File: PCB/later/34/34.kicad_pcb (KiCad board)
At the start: 2 copper layers, 112.4 x 93.3 mm, 61 parts, among them J1 USB_C_Receptacle_USB2.0, J2 Conn_01x04, J3 AVR-ISP-6, J4 Conn_01x04, SW1 SW_Push, SW10 SW_Push, SW11 SW_Push, SW12 SW_Push, SW13 SW_Push, SW14 SW_Push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

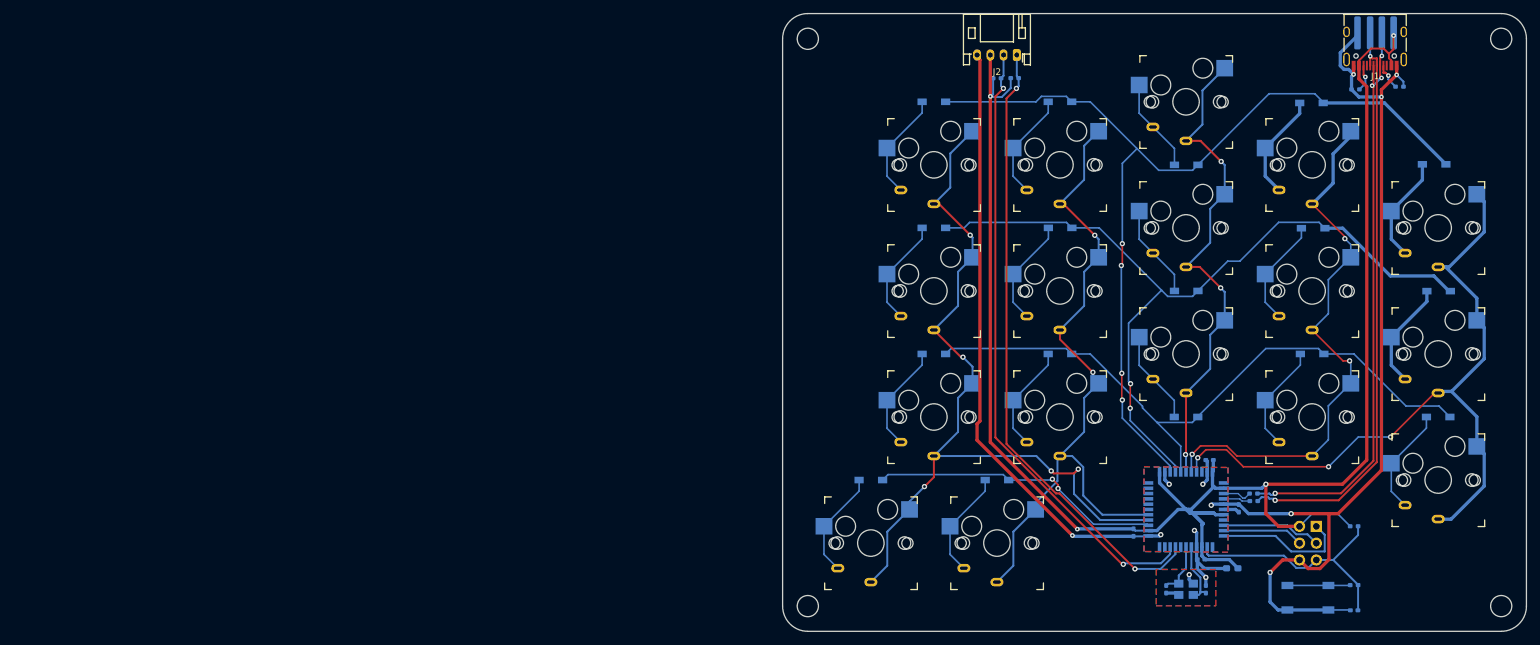
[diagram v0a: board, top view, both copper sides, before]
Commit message: postpone i2c design
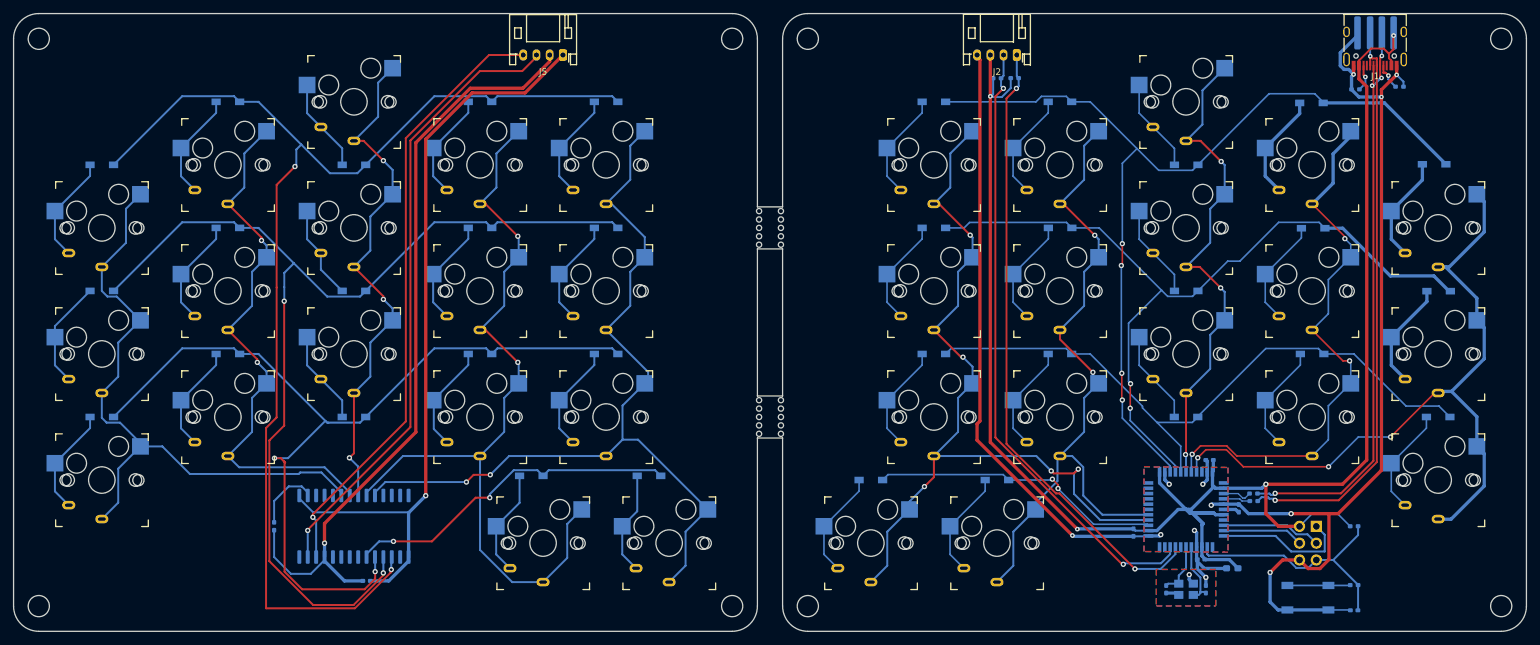
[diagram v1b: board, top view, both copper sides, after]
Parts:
- added C9: 0.1µF, Capacitor_SMD:C_0402_1005Metric_Pad0.74x0.62mm_HandSolder, B.Cu at (91.4, 131.4)
- added D18: 1N4148, Keyboard_Foostan:D3_SMD_v2, B.Cu at (51.4, 68.6)
- added D19: 1N4148, Keyboard_Foostan:D3_SMD_v2, B.Cu at (51.4, 87.6)
- added D20: 1N4148, Keyboard_Foostan:D3_SMD_v2, B.Cu at (51.4, 106.7)
- added D21: 1N4148, Keyboard_Foostan:D3_SMD_v2, B.Cu at (70.5, 59.1)
- added D22: 1N4148, Keyboard_Foostan:D3_SMD_v2, B.Cu at (70.5, 78.1)
- added D23: 1N4148, Keyboard_Foostan:D3_SMD_v2, B.Cu at (70.5, 97.2)
- added D24: 1N4148, Keyboard_Foostan:D3_SMD_v2, B.Cu at (89.5, 68.6)
- added D25: 1N4148, Keyboard_Foostan:D3_SMD_v2, B.Cu at (89.5, 87.6)
- added D26: 1N4148, Keyboard_Foostan:D3_SMD_v2, B.Cu at (89.5, 106.7)
- added D27: 1N4148, Keyboard_Foostan:D3_SMD_v2, B.Cu at (108.6, 59.1)
- added D28: 1N4148, Keyboard_Foostan:D3_SMD_v2, B.Cu at (108.6, 78.1)
- added D29: 1N4148, Keyboard_Foostan:D3_SMD_v2, B.Cu at (108.6, 97.2)
- added D30: 1N4148, Keyboard_Foostan:D3_SMD_v2, B.Cu at (116.3, 115.6)
- added D31: 1N4148, Keyboard_Foostan:D3_SMD_v2, B.Cu at (127.6, 59.1)
- added D32: 1N4148, Keyboard_Foostan:D3_SMD_v2, B.Cu at (127.6, 78.1)
- added D33: 1N4148, Keyboard_Foostan:D3_SMD_v2, B.Cu at (127.6, 97.2)
- added D34: 1N4148, Keyboard_Foostan:D3_SMD_v2, B.Cu at (134.1, 115.6)
- added J5: Conn_01x04, Connector_JST:JST_PH_S4B-PH-K_1x04_P2.00mm_Horizontal, F.Cu at (121.1, 52.0)
- added R9: 4k7Ω, Resistor_SMD:R_0402_1005Metric_Pad0.72x0.64mm_HandSolder, B.Cu at (77.5, 123.2)
- added REF**: breakaway-mousebites, Keyboard_Keebio-Parts:breakaway-mousebites, F.Cu at (150.5, 78.1)
- added REF**: breakaway-mousebites, Keyboard_Keebio-Parts:breakaway-mousebites, F.Cu at (150.5, 106.7)
- added REF**: MountingHole_3.2mm_M3_DIN965, MountingHole:MountingHole_3.2mm_M3_DIN965, F.Cu at (146.7, 49.5)
- added REF**: breakaway-mousebites, Keyboard_Keebio-Parts:breakaway-mousebites, F.Cu at (154.3, 78.1)
- added REF**: MountingHole_3.2mm_M3_DIN965, MountingHole:MountingHole_3.2mm_M3_DIN965, F.Cu at (41.9, 135.3)
- added REF**: breakaway-mousebites, Keyboard_Keebio-Parts:breakaway-mousebites, F.Cu at (154.3, 106.7)
- added REF**: MountingHole_3.2mm_M3_DIN965, MountingHole:MountingHole_3.2mm_M3_DIN965, F.Cu at (146.7, 135.3)
- added REF**: MountingHole_3.2mm_M3_DIN965, MountingHole:MountingHole_3.2mm_M3_DIN965, F.Cu at (41.9, 49.5)
- added SW19: SW_Push, Keyboard_JSA:MX_Hotswap_Choc_Solder, F.Cu at (51.4, 78.1)
- added SW20: SW_Push, Keyboard_JSA:MX_Hotswap_Choc_Solder, F.Cu at (51.4, 97.2)
- added SW21: SW_Push, Keyboard_JSA:MX_Hotswap_Choc_Solder, F.Cu at (51.4, 116.2)
- added SW22: SW_Push, Keyboard_JSA:MX_Hotswap_Choc_Solder, F.Cu at (70.5, 68.6)
- added SW23: SW_Push, Keyboard_JSA:MX_Hotswap_Choc_Solder, F.Cu at (70.5, 87.6)
- added SW24: SW_Push, Keyboard_JSA:MX_Hotswap_Choc_Solder, F.Cu at (70.5, 106.7)
- added SW25: SW_Push, Keyboard_JSA:MX_Hotswap_Choc_Solder, F.Cu at (89.5, 59.1)
- added SW26: SW_Push, Keyboard_JSA:MX_Hotswap_Choc_Solder, F.Cu at (89.5, 78.1)
- added SW27: SW_Push, Keyboard_JSA:MX_Hotswap_Choc_Solder, F.Cu at (89.5, 97.2)
- added SW28: SW_Push, Keyboard_JSA:MX_Hotswap_Choc_Solder, F.Cu at (108.6, 68.6)
- added SW29: SW_Push, Keyboard_JSA:MX_Hotswap_Choc_Solder, F.Cu at (108.6, 87.6)
- added SW30: SW_Push, Keyboard_JSA:MX_Hotswap_Choc_Solder, F.Cu at (108.6, 106.7)
- added SW31: SW_Push, Keyboard_JSA:MX_Hotswap_Choc_Solder, F.Cu at (118.1, 125.7)
- added SW32: SW_Push, Keyboard_JSA:MX_Hotswap_Choc_Solder, F.Cu at (127.6, 68.6)
- added SW33: SW_Push, Keyboard_JSA:MX_Hotswap_Choc_Solder, F.Cu at (127.6, 87.6)
- added SW34: SW_Push, Keyboard_JSA:MX_Hotswap_Choc_Solder, F.Cu at (127.6, 106.7)
- added SW35: SW_Push, Keyboard_JSA:MX_Hotswap_Choc_Solder, F.Cu at (137.2, 125.7)
- added U2: MCP23018_SO, Package_SO:SOIC-28W_7.5x17.9mm_P1.27mm, B.Cu at (89.5, 123.2)
- R8: value 4.7kΩ -> 4k7Ω
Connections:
- net Row1 renamed Row5
- net Row2 renamed Row6
- net Row3 renamed Row7
- net Row4 renamed Row8
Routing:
- net Row1: track 0.00 -> 187.0 mm, vias 0 -> 2
- net Row2: track 0.00 -> 162.0 mm, vias 0 -> 2
- net Row3: track 0.00 -> 138.3 mm, vias 0 -> 2
- net Col5: track 0.00 -> 128.1 mm, vias 0 -> 2
- net Col4: track 0.00 -> 119.5 mm, vias 0 -> 2
- net VDD: track 0.00 -> 115.2 mm, vias 0 -> 1
- net GND1: track 0.00 -> 114.7 mm, vias 0 -> 1
- net Col1: track 0.00 -> 96.6 mm
- net SDA1: track 0.00 -> 93.9 mm, vias 0 -> 1
- net SCL1: track 0.00 -> 92.3 mm, vias 0 -> 1
- net Col2: track 0.00 -> 82.3 mm, vias 0 -> 2
- net Col3: track 0.00 -> 78.3 mm, vias 0 -> 3
- net Row4: track 0.00 -> 51.5 mm, vias 0 -> 2
- net Net-(D33-Pad2): track 0.00 -> 16.4 mm
- net Net-(D32-Pad2): track 0.00 -> 16.4 mm
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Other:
- board size 112.4 x 93.3 mm -> 228.6 x 93.3 mm
